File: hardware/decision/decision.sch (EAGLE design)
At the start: 5 parts, among them IC1 7805T, IC2 A1301UA

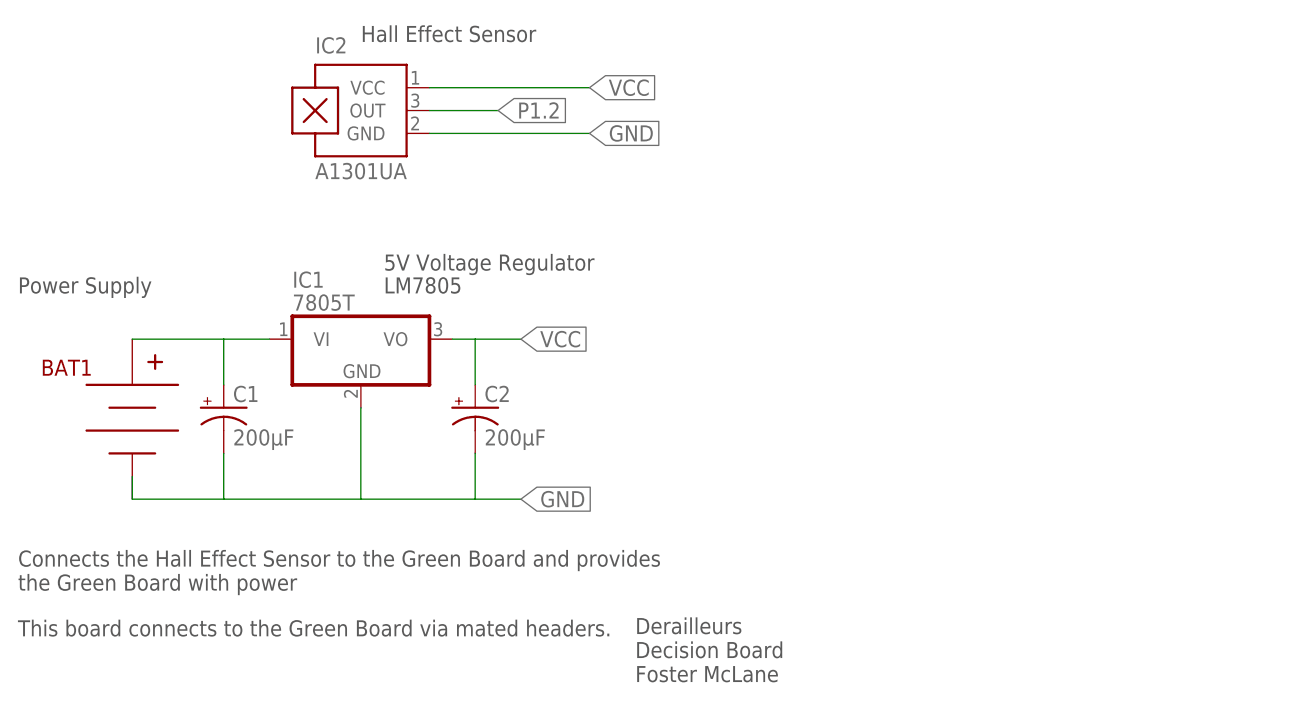
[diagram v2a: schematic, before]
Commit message: add decision board file
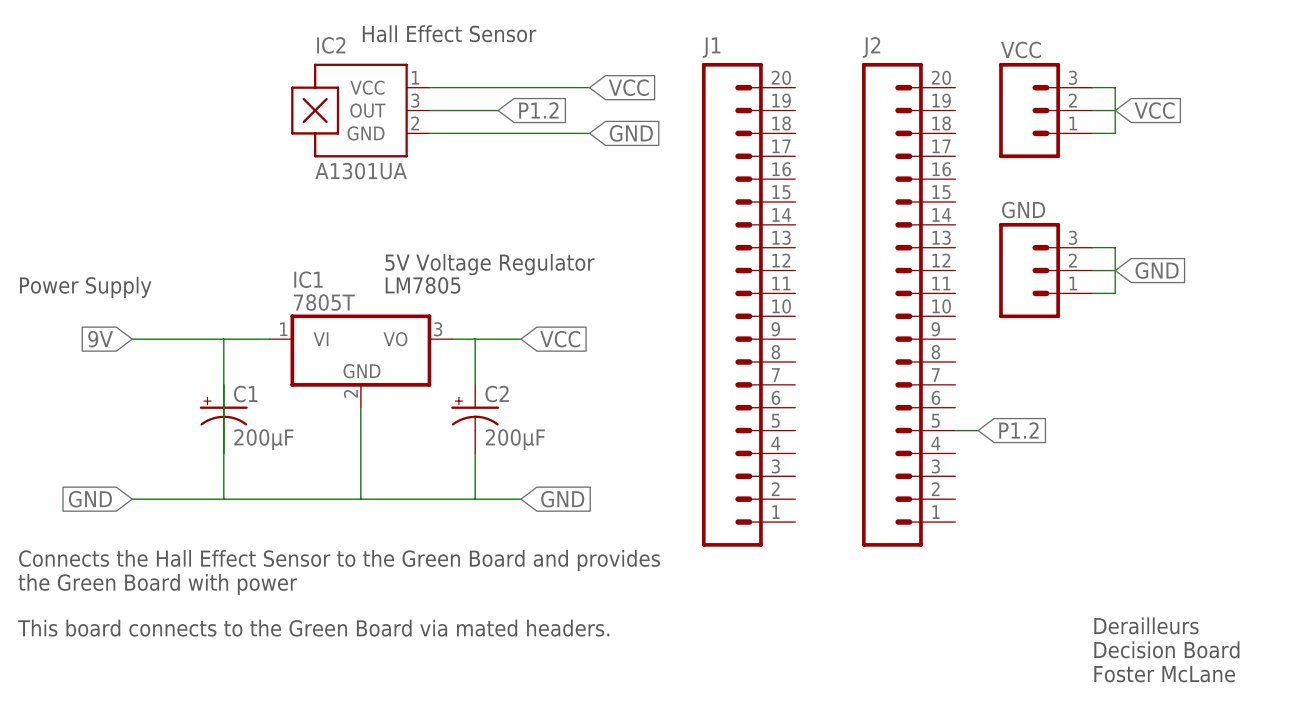
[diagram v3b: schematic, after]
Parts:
- removed BAT1: (no value), SparkFun-Connectors:BC9VPC
- added GND, VCC: (no value), SparkFun-Connectors:M03LOCK
- added J1, J2: (no value), SparkFun-Connectors:M20
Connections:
- new net 9V: C1.-, IC1.VI
- new net N$2: VCC.1, VCC.2, VCC.3
- net GND: now also C1.+; no longer C1.-
- net N$1: now also GND.1, GND.2, GND.3; no longer BAT1.V+, C1.+, IC1.VI
- net P1.2: now also J2.5
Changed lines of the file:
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@@
 </classes>
 <parts>
-<part name="BAT1" library="SparkFun-Connectors" deviceset="BC9VPC" device=""/>
 <part name="IC1" library="linear" deviceset="78*" device="T" technology="05"/>
 <part name="IC2" library="allegro" deviceset="A13*?" device="UA" technology="01"/>
 <part name="C1" library="SparkFun-Capacitors" deviceset="CAP_POL" device="PTH1" value="200µF"/>
 <part name="C2" library="SparkFun-Capacitors" deviceset="CAP_POL" device="PTH1" value="200µF"/>
+<part name="J1" library="SparkFun-Connectors" deviceset="M20" device=""/>
+<part name="J2" library="SparkFun-Connectors" deviceset="M20" device=""/>
+<part name="VCC" library="SparkFun-Connectors" deviceset="M03" device="LOCK"/>
+<part name="GND" library="SparkFun-Connectors" deviceset="M03" device="LOCK"/>
 </parts>
 <sheets>
@@
 <plain>
 <text x="45.72" y="27.94" size="1.778" layer="97">LM7805</text>
-<frame x1="-2.54" y1="-20.32" x2="96.52" y2="63.5" columns="8" rows="5" layer="91"/>
 <text x="43.18" y="55.88" size="1.778" layer="97">Hall Effect Sensor</text>
 <text x="45.72" y="30.48" size="1.778" layer="97">5V Voltage Regulator</text>
@@
 the Green Board with power</text>
 <text x="5.08" y="-10.16" size="1.778" layer="97">This board connects to the Green Board via mated headers.</text>
-<text x="73.66" y="-15.24" size="1.778" layer="97">Derailleurs
+<text x="124.46" y="-15.24" size="1.778" layer="97">Derailleurs
 Decision Board
 Foster McLane</text>
 <text x="5.08" y="27.94" size="1.778" layer="97">Power Supply</text>
+<frame x1="-12.7" y1="-22.86" x2="149.86" y2="68.58" columns="8" rows="5" layer="91"/>
 </plain>
 <instances>
-<instance part="BAT1" gate="G$1" x="17.78" y="15.24"/>
 <instance part="IC1" gate="A1" x="43.18" y="22.86"/>
 <instance part="IC2" gate="G$1" x="43.18" y="48.26"/>
 <instance part="C1" gate="G$1" x="27.94" y="15.24"/>
 <instance part="C2" gate="G$1" x="55.88" y="15.24"/>
+<instance part="J1" gate="G$1" x="81.28" y="-2.54"/>
+<instance part="J2" gate="G$1" x="99.06" y="-2.54"/>
+<instance part="VCC" gate="J$1" x="116.84" y="48.26"/>
+<instance part="GND" gate="J$1" x="116.84" y="30.48"/>
 </instances>
 <busses>
 </busses>
 <nets>
-<net name="N$1" class="0">
+<net name="9V" class="0">
 <segment>
-<pinref part="BAT1" gate="G$1" pin="V+"/>
 <pinref part="IC1" gate="A1" pin="VI"/>
 <wire x1="17.78" y1="22.86" x2="27.94" y2="22.86" width="0.1524" layer="91"/>
-<pinref part="C1" gate="G$1" pin="+"/>
+<pinref part="C1" gate="G$1" pin="-"/>
 <wire x1="27.94" y1="22.86" x2="33.02" y2="22.86" width="0.1524" layer="91"/>
-<wire x1="27.94" y1="17.78" x2="27.94" y2="22.86" width="0.1524" layer="91"/>
+<wire x1="27.94" y1="10.16" x2="27.94" y2="22.86" width="0.1524" layer="91"/>
+<label x="17.78" y="22.86" size="1.778" layer="95" rot="R180" xref="yes"/>
 </segment>
 </net>
@@
 <wire x1="43.18" y1="15.24" x2="43.18" y2="5.08" width="0.1524" layer="91"/>
 <wire x1="43.18" y1="5.08" x2="27.94" y2="5.08" width="0.1524" layer="91"/>
-<wire x1="27.94" y1="5.08" x2="17.78" y2="5.08" width="0.1524" layer="91"/>
-<wire x1="17.78" y1="5.08" x2="17.78" y2="7.62" width="0.1524" layer="91"/>
 <wire x1="43.18" y1="5.08" x2="55.88" y2="5.08" width="0.1524" layer="91"/>
 <label x="60.96" y="5.08" size="1.778" layer="95" xref="yes"/>
-<pinref part="C1" gate="G$1" pin="-"/>
+<pinref part="C1" gate="G$1" pin="+"/>
 <wire x1="55.88" y1="5.08" x2="60.96" y2="5.08" width="0.1524" layer="91"/>
-<wire x1="27.94" y1="10.16" x2="27.94" y2="5.08" width="0.1524" layer="91"/>
+<wire x1="27.94" y1="17.78" x2="27.94" y2="5.08" width="0.1524" layer="91"/>
 <pinref part="C2" gate="G$1" pin="-"/>
 <wire x1="55.88" y1="10.16" x2="55.88" y2="5.08" width="0.1524" layer="91"/>
+<wire x1="27.94" y1="5.08" x2="17.78" y2="5.08" width="0.1524" layer="91"/>
+<label x="127" y="30.48" size="1.778" layer="95" xref="yes"/>
+<label x="17.78" y="5.08" size="1.778" layer="95" rot="R180" xref="yes"/>
 </segment>
 <segment>
@@
 <wire x1="55.88" y1="22.86" x2="60.96" y2="22.86" width="0.1524" layer="91"/>
 <wire x1="55.88" y1="17.78" x2="55.88" y2="22.86" width="0.1524" layer="91"/>
+<label x="127" y="48.26" size="1.778" layer="95" xref="yes"/>
 </segment>
 <segment>
@@
 <label x="58.42" y="48.26" size="1.778" layer="95" xref="yes"/>
 </segment>
+<segment>
+<pinref part="J2" gate="G$1" pin="5"/>
+<wire x1="109.22" y1="12.7" x2="111.76" y2="12.7" width="0.1524" layer="91"/>
+<label x="111.76" y="12.7" size="1.778" layer="95" xref="yes"/>
+</segment>
 </net>
+<net name="N$1" class="0">
+<segment>
+<pinref part="GND" gate="J$1" pin="3"/>
+<wire x1="124.46" y1="33.02" x2="127" y2="33.02" width="0.1524" layer="91"/>
+<wire x1="127" y1="33.02" x2="127" y2="30.48" width="0.1524" layer="91"/>
+<pinref part="GND" gate="J$1" pin="2"/>
+<wire x1="127" y1="30.48" x2="124.46" y2="30.48" width="0.1524" layer="91"/>
+<pinref part="GND" gate="J$1" pin="1"/>
+<wire x1="124.46" y1="27.94" x2="127" y2="27.94" width="0.1524" layer="91"/>
+<wire x1="127" y1="27.94" x2="127" y2="30.48" width="0.1524" layer="91"/>
+</segment>
+</net>
+<net name="N$2" class="0">
+<segment>
+<pinref part="VCC" gate="J$1" pin="1"/>
+<wire x1="124.46" y1="45.72" x2="127" y2="45.72" width="0.1524" layer="91"/>
+<pinref part="VCC" gate="J$1" pin="3"/>
+<wire x1="124.46" y1="50.8" x2="127" y2="50.8" width="0.1524" layer="91"/>
+<wire x1="127" y1="50.8" x2="127" y2="48.26" width="0.1524" layer="91"/>
+<pinref part="VCC" gate="J$1" pin="2"/>
+<wire x1="127" y1="48.26" x2="127" y2="45.72" width="0.1524" layer="91"/>
+<wire x1="124.46" y1="48.26" x2="127" y2="48.26" width="0.1524" layer="91"/>
+</segment>
+</net>

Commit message: update decision board with proper nets
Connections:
- removed net N$1: GND.1, GND.2, GND.3
- removed net N$2: VCC.1, VCC.2, VCC.3
- net GND: now also GND.1, GND.2, GND.3
- net VCC: now also VCC.1, VCC.2, VCC.3
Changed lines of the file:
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@@
 <label x="68.58" y="45.72" size="1.778" layer="95" xref="yes"/>
+</segment>
+<segment>
+<pinref part="GND" gate="J$1" pin="3"/>
+<wire x1="124.46" y1="33.02" x2="127" y2="33.02" width="0.1524" layer="91"/>
+<wire x1="127" y1="33.02" x2="127" y2="30.48" width="0.1524" layer="91"/>
+<pinref part="GND" gate="J$1" pin="2"/>
+<wire x1="127" y1="30.48" x2="124.46" y2="30.48" width="0.1524" layer="91"/>
+<pinref part="GND" gate="J$1" pin="1"/>
+<wire x1="124.46" y1="27.94" x2="127" y2="27.94" width="0.1524" layer="91"/>
+<wire x1="127" y1="27.94" x2="127" y2="30.48" width="0.1524" layer="91"/>
 </segment>
 </net>
@@
 <label x="68.58" y="50.8" size="1.778" layer="95" xref="yes"/>
 </segment>
+<segment>
+<pinref part="VCC" gate="J$1" pin="1"/>
+<wire x1="124.46" y1="45.72" x2="127" y2="45.72" width="0.1524" layer="91"/>
+<pinref part="VCC" gate="J$1" pin="3"/>
+<wire x1="124.46" y1="50.8" x2="127" y2="50.8" width="0.1524" layer="91"/>
+<wire x1="127" y1="50.8" x2="127" y2="48.26" width="0.1524" layer="91"/>
+<pinref part="VCC" gate="J$1" pin="2"/>
+<wire x1="127" y1="48.26" x2="127" y2="45.72" width="0.1524" layer="91"/>
+<wire x1="124.46" y1="48.26" x2="127" y2="48.26" width="0.1524" layer="91"/>
+</segment>
 </net>
 <net name="P1.2" class="0">
@@
 </segment>
 </net>
-<net name="N$1" class="0">
-<segment>
-<pinref part="GND" gate="J$1" pin="3"/>
-<wire x1="124.46" y1="33.02" x2="127" y2="33.02" width="0.1524" layer="91"/>
-<wire x1="127" y1="33.02" x2="127" y2="30.48" width="0.1524" layer="91"/>
-<pinref part="GND" gate="J$1" pin="2"/>
-<wire x1="127" y1="30.48" x2="124.46" y2="30.48" width="0.1524" layer="91"/>
-<pinref part="GND" gate="J$1" pin="1"/>
-<wire x1="124.46" y1="27.94" x2="127" y2="27.94" width="0.1524" layer="91"/>
-<wire x1="127" y1="27.94" x2="127" y2="30.48" width="0.1524" layer="91"/>
-</segment>
-</net>
-<net name="N$2" class="0">
-<segment>
-<pinref part="VCC" gate="J$1" pin="1"/>
-<wire x1="124.46" y1="45.72" x2="127" y2="45.72" width="0.1524" layer="91"/>
-<pinref part="VCC" gate="J$1" pin="3"/>
-<wire x1="124.46" y1="50.8" x2="127" y2="50.8" width="0.1524" layer="91"/>
-<wire x1="127" y1="50.8" x2="127" y2="48.26" width="0.1524" layer="91"/>
-<pinref part="VCC" gate="J$1" pin="2"/>
-<wire x1="127" y1="48.26" x2="127" y2="45.72" width="0.1524" layer="91"/>
-<wire x1="124.46" y1="48.26" x2="127" y2="48.26" width="0.1524" layer="91"/>
-</segment>
-</net>

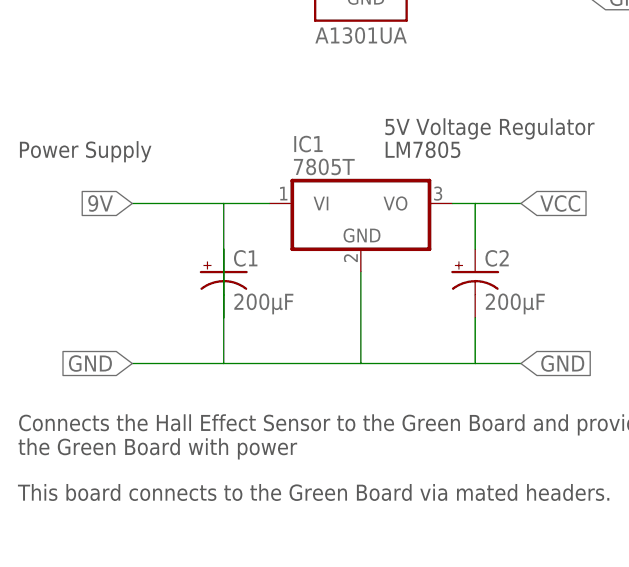
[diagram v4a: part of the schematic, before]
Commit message: update decision board with copper pools, silk screen, and proper routes
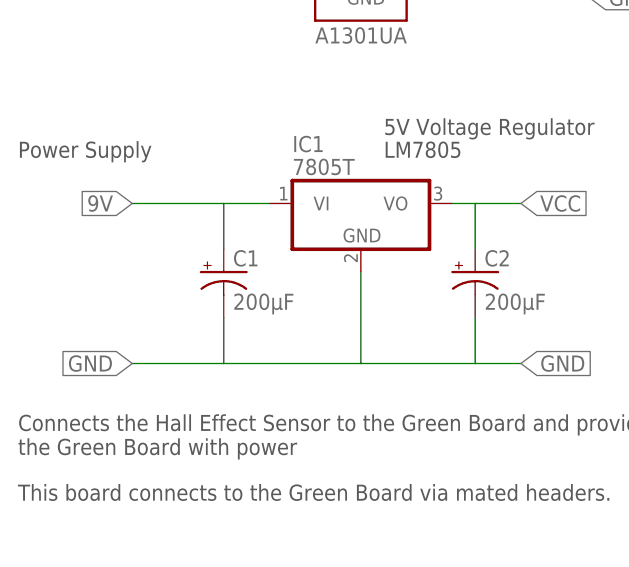
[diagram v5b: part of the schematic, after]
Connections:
- net 9V: now also C1.+; no longer C1.-
- net GND: now also C1.-; no longer C1.+
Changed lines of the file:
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@@
 <pinref part="IC1" gate="A1" pin="VI"/>
 <wire x1="17.78" y1="22.86" x2="27.94" y2="22.86" width="0.1524" layer="91"/>
-<pinref part="C1" gate="G$1" pin="-"/>
+<pinref part="C1" gate="G$1" pin="+"/>
 <wire x1="27.94" y1="22.86" x2="33.02" y2="22.86" width="0.1524" layer="91"/>
-<wire x1="27.94" y1="10.16" x2="27.94" y2="22.86" width="0.1524" layer="91"/>
+<wire x1="27.94" y1="17.78" x2="27.94" y2="22.86" width="0.1524" layer="91"/>
 <label x="17.78" y="22.86" size="1.778" layer="95" rot="R180" xref="yes"/>
 </segment>
@@
 <wire x1="43.18" y1="5.08" x2="55.88" y2="5.08" width="0.1524" layer="91"/>
 <label x="60.96" y="5.08" size="1.778" layer="95" xref="yes"/>
-<pinref part="C1" gate="G$1" pin="+"/>
+<pinref part="C1" gate="G$1" pin="-"/>
 <wire x1="55.88" y1="5.08" x2="60.96" y2="5.08" width="0.1524" layer="91"/>
-<wire x1="27.94" y1="17.78" x2="27.94" y2="5.08" width="0.1524" layer="91"/>
+<wire x1="27.94" y1="10.16" x2="27.94" y2="5.08" width="0.1524" layer="91"/>
 <pinref part="C2" gate="G$1" pin="-"/>
 <wire x1="55.88" y1="10.16" x2="55.88" y2="5.08" width="0.1524" layer="91"/>
